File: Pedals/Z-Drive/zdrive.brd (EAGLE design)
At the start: 53 x 53.3 mm, 28 parts, among them IC1 MC1458P, Q1 2N7000, Q2 2N7000

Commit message: Working on layout
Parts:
- removed D4: BAT41, SparkFun-DiscreteSemi:DIODE-1N4001-KIT
- added D5: BAT41, SparkFun-DiscreteSemi:DIODE-1N4001-KIT
- moved C4 67.1 mm to (24.1, 15.2)
- moved R7 64.1 mm to (15.2, 16.5), turned to 180 degrees
- moved C7 63.9 mm to (26.7, 8.89)
- moved R5 57.1 mm to (16.5, 6.35)
- moved C5 41.3 mm to (14.0, 10.2)
- moved IC1 33.4 mm to (15.2, 24.1), turned to 90 degrees
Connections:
- new net 9V: D5.A, IN.1
- net V+: now also D5.C; no longer D4.A, D4.C, IN.1

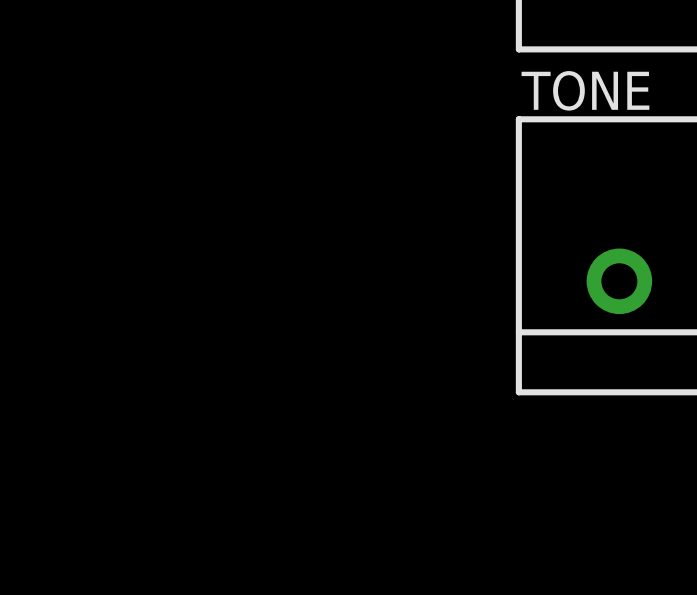
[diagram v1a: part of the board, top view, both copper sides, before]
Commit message: Adding switch for capacitor
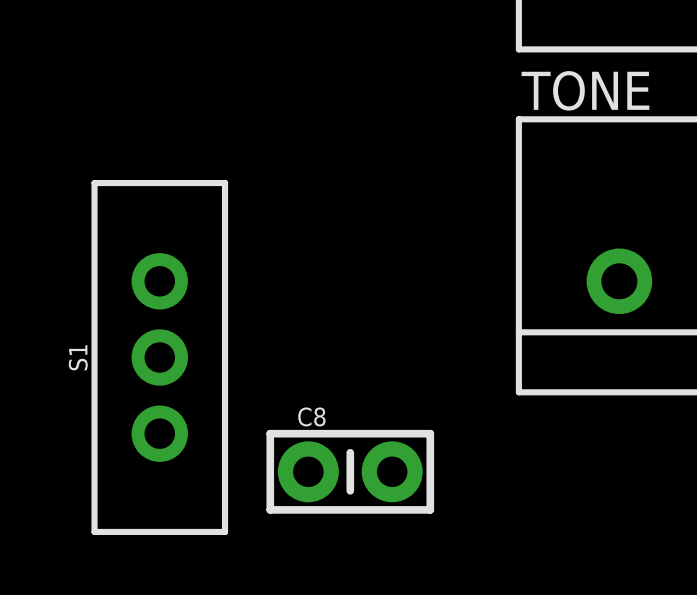
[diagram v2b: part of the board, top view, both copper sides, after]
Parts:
- added C8: 1NF, Custom-Parts:CAP-PTH-SMALL-KIT
- added S1: (no value), SparkFun-Switches:SWITCH_SPDT_PTH_11.6X4.0MM
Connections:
- new net N$11: C4.1, S1.3
- new net N$12: C8.1, S1.1
- net N$7: now also C8.2
- net V2: now also S1.2; no longer C4.1
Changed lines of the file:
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@@
 <attribute name="VALUE" x="6.604" y="11.43" size="0.6096" layer="27" font="vector" ratio="20" rot="R90" align="top-center"/>
+</element>
+<element name="C8" library="Custom-Parts" package="CAP-PTH-SMALL-KIT" value="1NF" x="-53.34" y="-2.54" smashed="yes">
+<attribute name="NAME" x="-55.118" y="-1.016" size="0.6096" layer="25"/>
+<attribute name="VALUE" x="-55.118" y="-4.572" size="0.6096" layer="27"/>
+</element>
+<element name="S1" library="SparkFun-Switches" library_urn="urn:adsk.eagle:library:535" package="SWITCH_SPDT_PTH_11.6X4.0MM" package3d_urn="urn:adsk.eagle:package:40177/1" value="" x="-59.69" y="1.27" smashed="yes">
+<attribute name="NAME" x="-62.103" y="1.27" size="0.6096" layer="25" font="vector" ratio="20" rot="R90" align="bottom-center"/>
+<attribute name="PROD_ID" value="SWCH-08261" x="-59.69" y="1.27" size="1.778" layer="27" display="off"/>
+<attribute name="SF_SKU" value="COM-00102" x="-59.69" y="1.27" size="1.778" layer="27" display="off"/>
+<attribute name="VALUE" x="-57.277" y="1.27" size="0.6096" layer="27" font="vector" ratio="20" rot="R90" align="top-center"/>
 </element>
 </elements>
@@
 </signal>
 <signal name="V2">
-<contactref element="C4" pad="1"/>
 <contactref element="R6" pad="P$2"/>
 <contactref element="R7" pad="P$1"/>
 <contactref element="C7" pad="1"/>
 <contactref element="R2" pad="P$2"/>
-<wire x1="34.29" y1="10.16" x2="34.29" y2="13.97" width="0" layer="19" extent="1-1"/>
-<wire x1="27.92" y1="8.89" x2="34.29" y2="10.16" width="0" layer="19" extent="1-1"/>
-<wire x1="22.733" y1="15.24" x2="27.92" y2="8.89" width="0" layer="19" extent="1-1"/>
-<wire x1="19.05" y1="16.51" x2="22.733" y2="15.24" width="0" layer="19" extent="1-1"/>
+<contactref element="S1" pad="2"/>
+<wire x1="19.05" y1="16.51" x2="-59.69" y2="1.27" width="0" layer="19" extent="1-1"/>
+<wire x1="27.92" y1="8.89" x2="19.05" y2="16.51" width="0" layer="19" extent="1-1"/>
+<wire x1="34.29" y1="10.16" x2="27.92" y2="8.89" width="0" layer="19" extent="1-1"/>
+<wire x1="34.29" y1="13.97" x2="34.29" y2="10.16" width="0" layer="19" extent="1-1"/>
 </signal>
 <signal name="N$6">
@@
 </signal>
 <signal name="N$7">
-<contactref element="C4" pad="2"/>
 <contactref element="VOICE" pad="1"/>
 <contactref element="VOICE" pad="2"/>
-<wire x1="-21.59" y1="15.24" x2="25.527" y2="15.24" width="0" layer="19" extent="1-1"/>
-<wire x1="-26.59" y1="15.24" x2="-21.59" y2="15.24" width="0" layer="19" extent="1-1"/>
+<contactref element="C8" pad="2"/>
+<contactref element="C4" pad="2"/>
+<wire x1="-26.59" y1="15.24" x2="-51.943" y2="-2.54" width="0" layer="19" extent="1-1"/>
+<wire x1="-21.59" y1="15.24" x2="-26.59" y2="15.24" width="0" layer="19" extent="1-1"/>
+<wire x1="25.527" y1="15.24" x2="-21.59" y2="15.24" width="0" layer="19" extent="1-1"/>
 </signal>
 <signal name="N$8">
@@
 <wire x1="5.08" y1="2.54" x2="5.08" y2="6.35" width="0" layer="19" extent="1-1"/>
 </signal>
+<signal name="N$11">
+<contactref element="S1" pad="3"/>
+<contactref element="C4" pad="1"/>
+<wire x1="22.733" y1="15.24" x2="-59.69" y2="-1.27" width="0" layer="19" extent="1-1"/>
+</signal>
+<signal name="N$12">
+<contactref element="S1" pad="1"/>
+<contactref element="C8" pad="1"/>
+<wire x1="-54.737" y1="-2.54" x2="-59.69" y2="3.81" width="0" layer="19" extent="1-1"/>
+</signal>
 </signals>

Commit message: Working on board layout
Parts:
- moved GAIN 99.4 mm to (62.2, 57.1), turned to 270 degrees
- moved VOL 97.1 mm to (47.0, 59.7), turned to 90 degrees
- moved TONE 93.4 mm to (47.0, 39.4), turned to 90 degrees
- moved C3 88.2 mm to (27.9, 59.7)
- moved VOICE 87.2 mm to (62.2, 39.4), turned to 270 degrees
- moved R4 81.5 mm to (33.0, 54.6)
- moved C2 76.2 mm to (29.2, 22.9), turned to 180 degrees
- moved C8 75.6 mm to (21.6, 7.62)
- moved S1 75.5 mm to (15.2, 10.2), turned to 180 degrees
- moved R8 74.5 mm to (24.1, 69.8), turned to 180 degrees
- moved R3 64.7 mm to (24.1, 66.0)
- moved Q1 60.9 mm to (14.0, 68.6), turned to 180 degrees
- moved R5 55.9 mm to (68.6, 26.7), turned to 180 degrees
- moved Q2 54.6 mm to (5.08, 45.7)
- moved C1 52.1 mm to (11.4, 22.9)
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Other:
- board size 53 x 53.3 mm -> 77.1 x 73.7 mm

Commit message: Restarting board design...
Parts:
- moved GAIN 104.8 mm to (-27.9, 3.81), turned to 0 degrees
- moved TONE 99.3 mm to (-45.7, 3.81), turned to 0 degrees
- moved OUT 98.3 mm to (-24.1, 57.1)
- moved VOL 96.6 mm to (-39.4, 16.5), turned to 0 degrees
- moved R5 90.4 mm to (-17.8, 53.3), turned to 0 degrees
- moved C3 87.7 mm to (-53.3, 26.7)
- moved VOICE 86.9 mm to (-21.6, 16.5), turned to 0 degrees
- moved R6 83.9 mm to (-27.9, 53.3), turned to 0 degrees
- moved R4 81.4 mm to (-48.3, 49.5)
- moved C5 77.5 mm to (-16.5, 39.4), turned to 0 degrees
- moved C2 76.3 mm to (-47.0, 26.7), turned to 0 degrees
- moved R8 74.2 mm to (-48.3, 53.3), turned to 0 degrees
- moved C6 73.5 mm to (-26.7, 29.2), flipped to the top, turned to 0 degrees
- moved C4 67.5 mm to (-29.2, 57.1)
- moved R2 66.2 mm to (-27.9, 49.5), turned to 0 degrees
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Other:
- board size 77.1 x 73.7 mm -> 55.5 x 54.6 mm

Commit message: Working on board layout
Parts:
- moved TONE 70.0 mm to (22.9, 17.8), turned to 90 degrees
- moved VOL 65.1 mm to (22.9, 35.6), turned to 90 degrees
- moved GAIN 61.3 mm to (31.8, 17.8), turned to 270 degrees
- moved S1 58.4 mm to (26.7, 47.0), turned to 270 degrees
- moved VOICE 56.6 mm to (31.8, 35.6), turned to 270 degrees
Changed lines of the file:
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@@
 <attribute name="VALUE" x="-31.75" y="42.926" size="0.6096" layer="27" font="vector" ratio="20" align="top-center"/>
 </element>
-<element name="GAIN" library="Custom-Parts" package="3RP/1610N" package3d_urn="urn:adsk.eagle:package:22726/1" value="B500k" x="-27.94" y="3.81" smashed="yes">
-<attribute name="NAME" x="-36.195" y="9.525" size="1.27" layer="25"/>
-<attribute name="POPULARITY" value="8" x="0" y="0" size="1.778" layer="27" display="off"/>
-<attribute name="VALUE" x="-31.115" y="6.35" size="1.27" layer="27"/>
+<element name="GAIN" library="Custom-Parts" package="3RP/1610N" package3d_urn="urn:adsk.eagle:package:22726/1" value="B500k" x="31.75" y="17.78" smashed="yes" rot="R270">
+<attribute name="NAME" x="37.465" y="26.035" size="1.27" layer="25" rot="R270"/>
+<attribute name="POPULARITY" value="8" x="27.94" y="-10.16" size="1.778" layer="27" rot="R270" display="off"/>
+<attribute name="VALUE" x="34.29" y="20.955" size="1.27" layer="27" rot="R270"/>
 </element>
 <element name="IC1" library="SamacSys_Parts" package="DIP794W53P254L959H508Q8N" value="MC1458P" x="-17.78" y="30.48" smashed="yes">
@@
 <attribute name="VALUE" x="-48.26" y="52.324" size="0.6096" layer="27" font="vector" ratio="20" align="top-center"/>
 </element>
-<element name="S1" library="SparkFun-Switches" library_urn="urn:adsk.eagle:library:535" package="SWITCH_SPDT_PTH_11.6X4.0MM" package3d_urn="urn:adsk.eagle:package:40177/1" value="" x="-15.24" y="6.35" smashed="yes">
-<attribute name="NAME" x="-17.653" y="6.35" size="0.6096" layer="25" font="vector" ratio="20" rot="R90" align="bottom-center"/>
-<attribute name="PROD_ID" value="SWCH-08261" x="0" y="0" size="1.778" layer="27" display="off"/>
-<attribute name="SF_SKU" value="COM-00102" x="0" y="0" size="1.778" layer="27" display="off"/>
-<attribute name="VALUE" x="-12.827" y="6.35" size="0.6096" layer="27" font="vector" ratio="20" rot="R90" align="top-center"/>
-</element>
-<element name="TONE" library="Custom-Parts" package="3RP/1610N" package3d_urn="urn:adsk.eagle:package:22726/1" value="B50k" x="-45.72" y="3.81" smashed="yes">
-<attribute name="NAME" x="-53.975" y="9.525" size="1.27" layer="25"/>
-<attribute name="POPULARITY" value="8" x="0" y="0" size="1.778" layer="27" display="off"/>
-<attribute name="VALUE" x="-48.895" y="6.35" size="1.27" layer="27"/>
-</element>
-<element name="VOICE" library="Custom-Parts" package="3RP/1610N" package3d_urn="urn:adsk.eagle:package:22726/1" value="B10k" x="-21.59" y="16.51" smashed="yes">
-<attribute name="NAME" x="-29.845" y="22.225" size="1.27" layer="25"/>
-<attribute name="POPULARITY" value="8" x="0" y="0" size="1.778" layer="27" display="off"/>
-<attribute name="VALUE" x="-24.765" y="19.05" size="1.27" layer="27"/>
-</element>
-<element name="VOL" library="Custom-Parts" package="3RP/1610N" package3d_urn="urn:adsk.eagle:package:22726/1" value="B100k" x="-39.37" y="16.51" smashed="yes">
-<attribute name="NAME" x="-47.625" y="22.225" size="1.27" layer="25"/>
-<attribute name="POPULARITY" value="8" x="0" y="0" size="1.778" layer="27" display="off"/>
-<attribute name="VALUE" x="-42.545" y="19.05" size="1.27" layer="27"/>
+<element name="S1" library="SparkFun-Switches" library_urn="urn:adsk.eagle:library:535" package="SWITCH_SPDT_PTH_11.6X4.0MM" package3d_urn="urn:adsk.eagle:package:40177/1" value="" x="26.67" y="46.99" smashed="yes" rot="R270">
+<attribute name="NAME" x="26.67" y="49.403" size="0.6096" layer="25" font="vector" ratio="20" align="bottom-center"/>
+<attribute name="PROD_ID" value="SWCH-08261" x="20.32" y="31.75" size="1.778" layer="27" rot="R270" display="off"/>
+<attribute name="SF_SKU" value="COM-00102" x="20.32" y="31.75" size="1.778" layer="27" rot="R270" display="off"/>
+<attribute name="VALUE" x="26.67" y="44.577" size="0.6096" layer="27" font="vector" ratio="20" align="top-center"/>
+</element>
+<element name="TONE" library="Custom-Parts" package="3RP/1610N" package3d_urn="urn:adsk.eagle:package:22726/1" value="B50k" x="22.86" y="17.78" smashed="yes" rot="R90">
+<attribute name="NAME" x="17.145" y="9.525" size="1.27" layer="25" rot="R90"/>
+<attribute name="POPULARITY" value="8" x="26.67" y="63.5" size="1.778" layer="27" rot="R90" display="off"/>
+<attribute name="VALUE" x="20.32" y="14.605" size="1.27" layer="27" rot="R90"/>
+</element>
+<element name="VOICE" library="Custom-Parts" package="3RP/1610N" package3d_urn="urn:adsk.eagle:package:22726/1" value="B10k" x="31.75" y="35.56" smashed="yes" rot="R270">
+<attribute name="NAME" x="37.465" y="43.815" size="1.27" layer="25" rot="R270"/>
+<attribute name="POPULARITY" value="8" x="15.24" y="13.97" size="1.778" layer="27" rot="R270" display="off"/>
+<attribute name="VALUE" x="34.29" y="38.735" size="1.27" layer="27" rot="R270"/>
+</element>
+<element name="VOL" library="Custom-Parts" package="3RP/1610N" package3d_urn="urn:adsk.eagle:package:22726/1" value="B100k" x="22.86" y="35.56" smashed="yes" rot="R90">
+<attribute name="NAME" x="17.145" y="27.305" size="1.27" layer="25" rot="R90"/>
+<attribute name="POPULARITY" value="8" x="39.37" y="74.93" size="1.778" layer="27" rot="R90" display="off"/>
+<attribute name="VALUE" x="20.32" y="32.385" size="1.27" layer="27" rot="R90"/>
 </element>
 </elements>
@@
 <wire x1="-35.54" y1="29.21" x2="-27.92" y2="29.21" width="0" layer="19" extent="1-1"/>
 <wire x1="-45.593" y1="26.67" x2="-35.54" y2="29.21" width="0" layer="19" extent="1-1"/>
-<wire x1="-34.37" y1="16.51" x2="-35.54" y2="29.21" width="0" layer="19" extent="1-1"/>
+<wire x1="22.86" y1="40.56" x2="-35.54" y2="29.21" width="0" layer="19" extent="1-1"/>
 </signal>
 <signal name="IN">
@@
 <wire x1="-44.45" y1="45.72" x2="-41.91" y2="49.53" width="0" layer="19" extent="1-1"/>
 <wire x1="-43.18" y1="44.45" x2="-44.45" y2="45.72" width="0" layer="19" extent="1-1"/>
-<wire x1="-22.94" y1="3.81" x2="-21.75" y2="34.29" width="0" layer="19" extent="1-1"/>
+<wire x1="31.75" y1="12.78" x2="-21.75" y2="34.29" width="0" layer="19" extent="1-1"/>
 </signal>
 <signal name="N$1">
 <contactref element="R3" pad="P$2"/>
 <contactref element="TONE" pad="1"/>
-<wire x1="-34.29" y1="49.53" x2="-50.72" y2="3.81" width="0" layer="19" extent="1-1"/>
+<wire x1="-34.29" y1="49.53" x2="22.86" y2="12.78" width="0" layer="19" extent="1-1"/>
 </signal>
 <signal name="OP5">
@@
 <contactref element="TONE" pad="2"/>
 <contactref element="IC1" pad="5"/>
-<wire x1="-40.72" y1="3.81" x2="-45.72" y2="3.81" width="0" layer="19" extent="1-1"/>
-<wire x1="-48.387" y1="26.67" x2="-45.72" y2="3.81" width="0" layer="19" extent="1-1"/>
+<wire x1="22.86" y1="22.78" x2="22.86" y2="17.78" width="0" layer="19" extent="1-1"/>
+<wire x1="-48.387" y1="26.67" x2="22.86" y2="17.78" width="0" layer="19" extent="1-1"/>
 <wire x1="-13.81" y1="26.67" x2="-48.387" y2="26.67" width="0" layer="19" extent="1-1"/>
 </signal>
@@
 <contactref element="R4" pad="P$2"/>
 <contactref element="VOL" pad="1"/>
-<wire x1="-44.45" y1="49.53" x2="-44.37" y2="16.51" width="0" layer="19" extent="1-1"/>
+<wire x1="-44.45" y1="49.53" x2="22.86" y2="30.56" width="0" layer="19" extent="1-1"/>
 </signal>
 <signal name="V2">
@@
 <wire x1="-41.91" y1="53.34" x2="-24.13" y2="53.34" width="0" layer="19" extent="1-1"/>
 <wire x1="-33.04" y1="29.21" x2="-24.13" y2="49.53" width="0" layer="19" extent="1-1"/>
-<wire x1="-15.24" y1="6.35" x2="-33.04" y2="29.21" width="0" layer="19" extent="1-1"/>
+<wire x1="26.67" y1="46.99" x2="-33.04" y2="29.21" width="0" layer="19" extent="1-1"/>
 </signal>
 <signal name="N$6">
 <contactref element="R5" pad="P$1"/>
 <contactref element="VOICE" pad="3"/>
-<wire x1="-16.59" y1="16.51" x2="-21.59" y2="53.34" width="0" layer="19" extent="1-1"/>
+<wire x1="31.75" y1="30.56" x2="-21.59" y2="53.34" width="0" layer="19" extent="1-1"/>
 </signal>
 <signal name="N$7">
@@
 <contactref element="C4" pad="2"/>
 <wire x1="-21.463" y1="39.37" x2="-27.813" y2="57.15" width="0" layer="19" extent="1-1"/>
-<wire x1="-21.59" y1="16.51" x2="-21.463" y2="39.37" width="0" layer="19" extent="1-1"/>
-<wire x1="-26.59" y1="16.51" x2="-21.59" y2="16.51" width="0" layer="19" extent="1-1"/>
+<wire x1="31.75" y1="35.56" x2="-21.463" y2="39.37" width="0" layer="19" extent="1-1"/>
+<wire x1="31.75" y1="40.56" x2="31.75" y2="35.56" width="0" layer="19" extent="1-1"/>
 </signal>
 <signal name="N$8">
@@
 <wire x1="-50.8" y1="44.45" x2="-36.83" y2="39.37" width="0" layer="19" extent="1-1"/>
 <wire x1="-52.07" y1="45.72" x2="-50.8" y2="44.45" width="0" layer="19" extent="1-1"/>
-<wire x1="-32.94" y1="3.81" x2="-21.75" y2="31.75" width="0" layer="19" extent="1-1"/>
+<wire x1="31.75" y1="22.78" x2="-21.75" y2="31.75" width="0" layer="19" extent="1-1"/>
 </signal>
 <signal name="N$5">
 <contactref element="R8" pad="P$1"/>
 <contactref element="GAIN" pad="2"/>
-<wire x1="-52.07" y1="53.34" x2="-27.94" y2="3.81" width="0" layer="19" extent="1-1"/>
+<wire x1="-52.07" y1="53.34" x2="31.75" y2="17.78" width="0" layer="19" extent="1-1"/>
 </signal>
 <signal name="OUT">
 <contactref element="VOL" pad="2"/>
 <contactref element="OUT" pad="2"/>
-<wire x1="-39.37" y1="16.51" x2="-21.59" y2="57.15" width="0" layer="19" extent="1-1"/>
+<wire x1="22.86" y1="35.56" x2="-21.59" y2="57.15" width="0" layer="19" extent="1-1"/>
 </signal>
 <signal name="9V">
@@
 <contactref element="S1" pad="3"/>
 <contactref element="C4" pad="1"/>
-<wire x1="-15.24" y1="3.81" x2="-30.607" y2="57.15" width="0" layer="19" extent="1-1"/>
+<wire x1="24.13" y1="46.99" x2="-30.607" y2="57.15" width="0" layer="19" extent="1-1"/>
 </signal>
 <signal name="N$12">
 <contactref element="S1" pad="1"/>
 <contactref element="C8" pad="1"/>
-<wire x1="-15.24" y1="8.89" x2="-24.257" y2="39.37" width="0" layer="19" extent="1-1"/>
+<wire x1="29.21" y1="46.99" x2="-24.257" y2="39.37" width="0" layer="19" extent="1-1"/>
 </signal>
 </signals>

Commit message: Working on board layout
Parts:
- moved OUT 92.7 mm to (50.8, 2.54)
- moved C7 81.1 mm to (43.2, 5.08)
- moved R1 65.6 mm to (27.9, 2.54), turned to 180 degrees
- moved IN 58.7 mm to (3.81, 2.54)
- moved Q2 58.5 mm to (8.89, 41.9), turned to 90 degrees
- moved D5 47.6 mm to (2.54, 11.4), turned to 90 degrees
- moved C6 46.2 mm to (12.7, 5.08)
- moved Q1 46.2 mm to (3.81, 39.4), turned to 270 degrees
- moved IC1 27.7 mm to (8.89, 22.9), turned to 270 degrees
- moved VOICE 22.2 mm to (22.9, 15.2), turned to 90 degrees
- moved GAIN 17.6 mm to (22.9, 33.0), turned to 90 degrees
- moved TONE 9.25 mm to (31.8, 15.2), turned to 270 degrees
- moved VOL 9.25 mm to (31.8, 33.0), turned to 270 degrees
- moved S1 2.54 mm to (26.7, 44.5)

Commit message: Working on board layout
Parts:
- moved C3 105.4 mm to (52.1, 27.9), turned to 90 degrees
- moved D2 99.5 mm to (52.1, 15.2), turned to 90 degrees
- moved R4 98.6 mm to (49.5, 36.8), turned to 90 degrees
- moved R8 91.7 mm to (41.9, 36.8), turned to 90 degrees
- moved R3 84.8 mm to (45.7, 36.8), turned to 270 degrees
- moved D3 72.2 mm to (47.0, 15.2), turned to 270 degrees
- moved C5 65.8 mm to (48.3, 27.9), turned to 90 degrees
- moved C2 61.6 mm to (12.7, 11.4), turned to 90 degrees
- moved C8 55.5 mm to (31.8, 49.5), turned to 180 degrees
- moved C4 51.4 mm to (21.6, 49.5), turned to 180 degrees
- moved R7 50.8 mm to (2.54, 22.9), turned to 270 degrees
- moved C1 50.6 mm to (7.62, 11.4), turned to 270 degrees
- moved R6 43.5 mm to (15.2, 48.3), turned to 270 degrees
- moved R5 38.6 mm to (16.5, 35.6), turned to 90 degrees
- moved D1 38.3 mm to (6.35, 35.6), turned to 90 degrees
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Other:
- board size 55.5 x 54.6 mm -> 55.9 x 54.6 mm

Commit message: Working on routing
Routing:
- net GND: track 0.00 -> 143.1 mm
- net V2: track 0.00 -> 99.1 mm
- net OP1: track 0.00 -> 74.0 mm
- net OP2: track 0.00 -> 71.8 mm
- net N$2: track 0.00 -> 59.0 mm
- net N$9: track 0.00 -> 52.7 mm
- net N$7: track 0.00 -> 50.6 mm
- net OP3: track 0.00 -> 40.7 mm
- net OUT: track 0.00 -> 39.9 mm
- net OP5: track 0.00 -> 36.1 mm
- net IN: track 0.00 -> 25.8 mm
- net N$5: track 0.00 -> 20.3 mm
- net N$1: track 0.00 -> 19.3 mm
- net N$4: track 0.00 -> 18.9 mm
- net N$6: track 0.00 -> 14.1 mm
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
